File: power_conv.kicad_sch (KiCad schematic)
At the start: 28 parts, among them IC1 MAX17262HEWL+T, U10 TPS22916CNYFPR, U7 TPS62840YBGR, U8 TPS62840YBGR

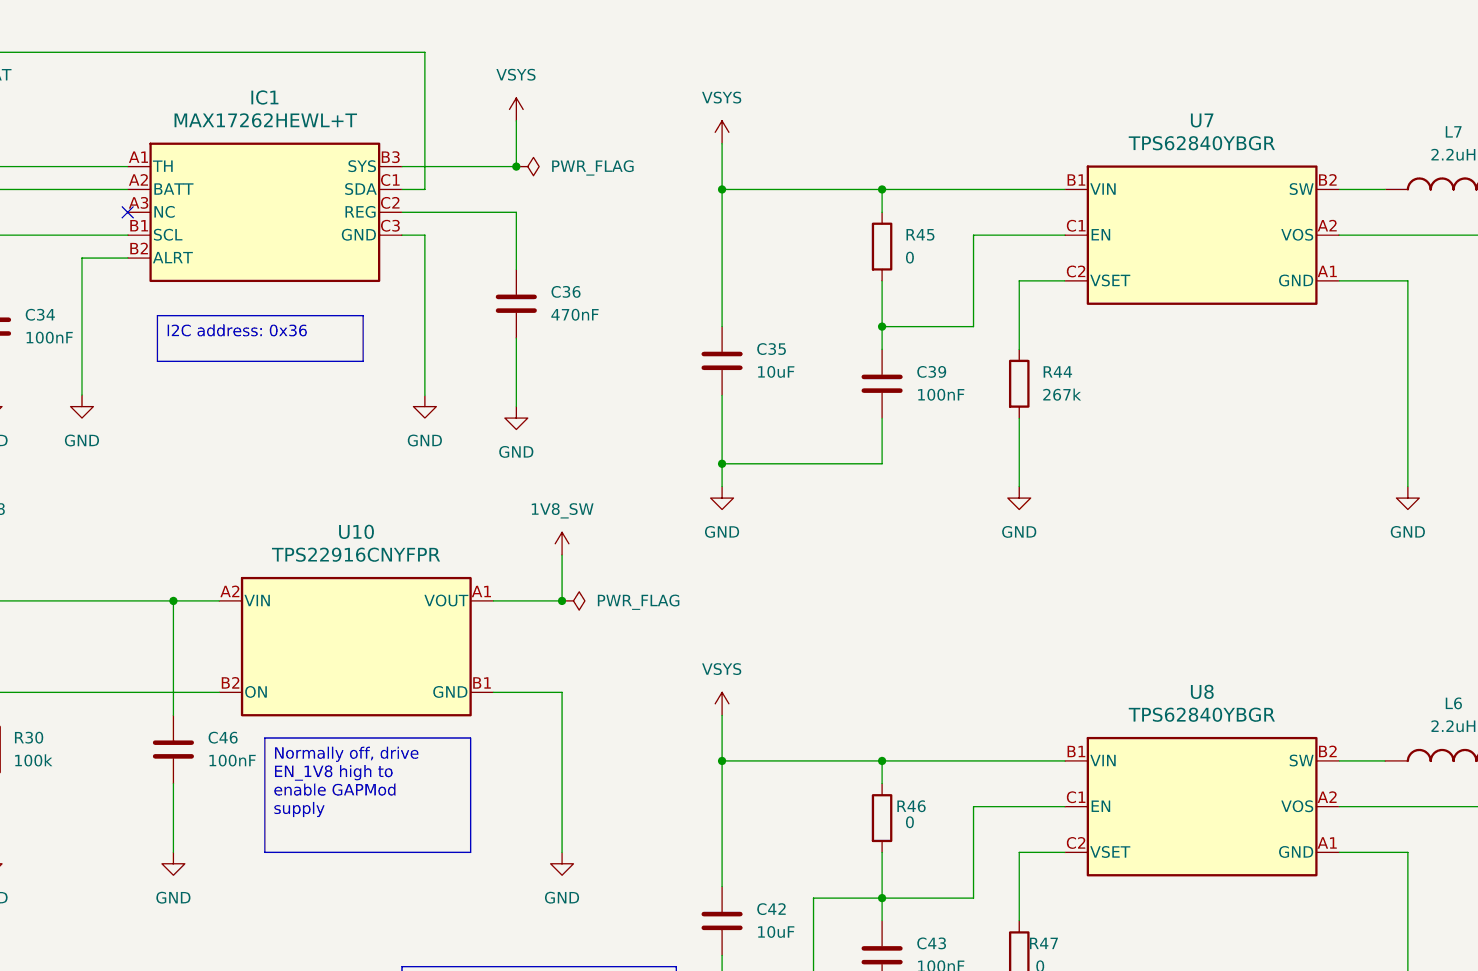
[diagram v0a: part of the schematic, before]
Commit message: added schematics comments of review 1
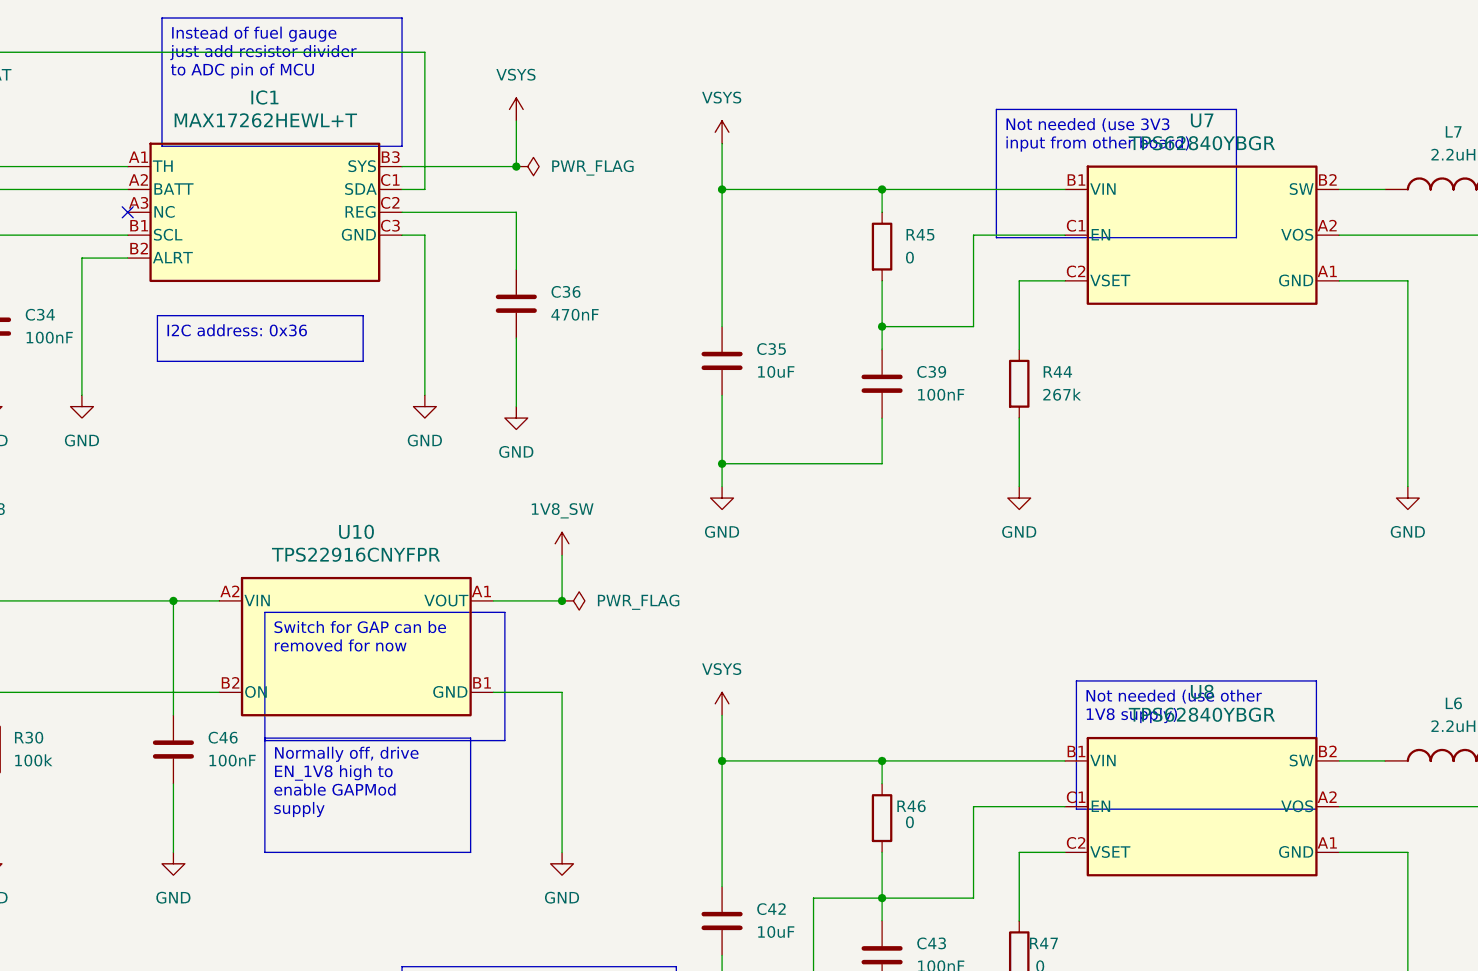
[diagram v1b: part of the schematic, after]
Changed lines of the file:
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@@
+		)
+	)
+	(text_box "Not needed (use 3V3 input from other board) "
+		(exclude_from_sim no)
+		(at 172.72 31.75 0)
+		(size 26.67 14.2494)
+		(margins 0.9525 0.9525 0.9525 0.9525)
+		(stroke
+			(width 0)
+			(type solid)
+		)
+		(fill
+			(type color)
+			(color 255 153 0 1)
+		)
+		(effects
+			(font
+				(size 1.27 1.27)
+			)
+			(justify left top)
 		)
 	)
@@
 			(type color)
 			(color 255 255 150 1)
+		)
+		(effects
+			(font
+				(size 1.27 1.27)
+			)
+			(justify left top)
+		)
+	)
+	(text_box "Not needed (use other 1V8 supply) "
+		(exclude_from_sim no)
+		(at 181.61 95.25 0)
+		(size 26.67 14.2494)
+		(margins 0.9525 0.9525 0.9525 0.9525)
+		(stroke
+			(width 0)
+			(type solid)
+		)
+		(fill
+			(type color)
+			(color 255 153 0 1)
 		)
 		(effects
@@
 		)
 		(effects
+			(font
+				(size 1.27 1.27)
+			)
+			(justify left top)
+		)
+	)
+	(text_box "Switch for GAP can be removed for now"
+		(exclude_from_sim no)
+		(at 91.44 87.63 0)
+		(size 26.67 14.2494)
+		(margins 0.9525 0.9525 0.9525 0.9525)
+		(stroke
+			(width 0)
+			(type solid)
+		)
+		(fill
+			(type color)
+			(color 255 153 0 1)
+		)
+		(effects
+			(font
+				(size 1.27 1.27)
+			)
+			(justify left top)
+		)
+	)
+	(text_box "Instead of fuel gauge just add resistor divider to ADC pin of MCU"
+		(exclude_from_sim no)
+		(at 80.01 21.59 0)
+		(size 26.67 14.2494)
+		(margins 0.9525 0.9525 0.9525 0.9525)
+		(stroke
+			(width 0)
+			(type solid)
+		)
+		(fill
+			(type color)
+			(color 255 153 0 1)
+		)
+		(effects

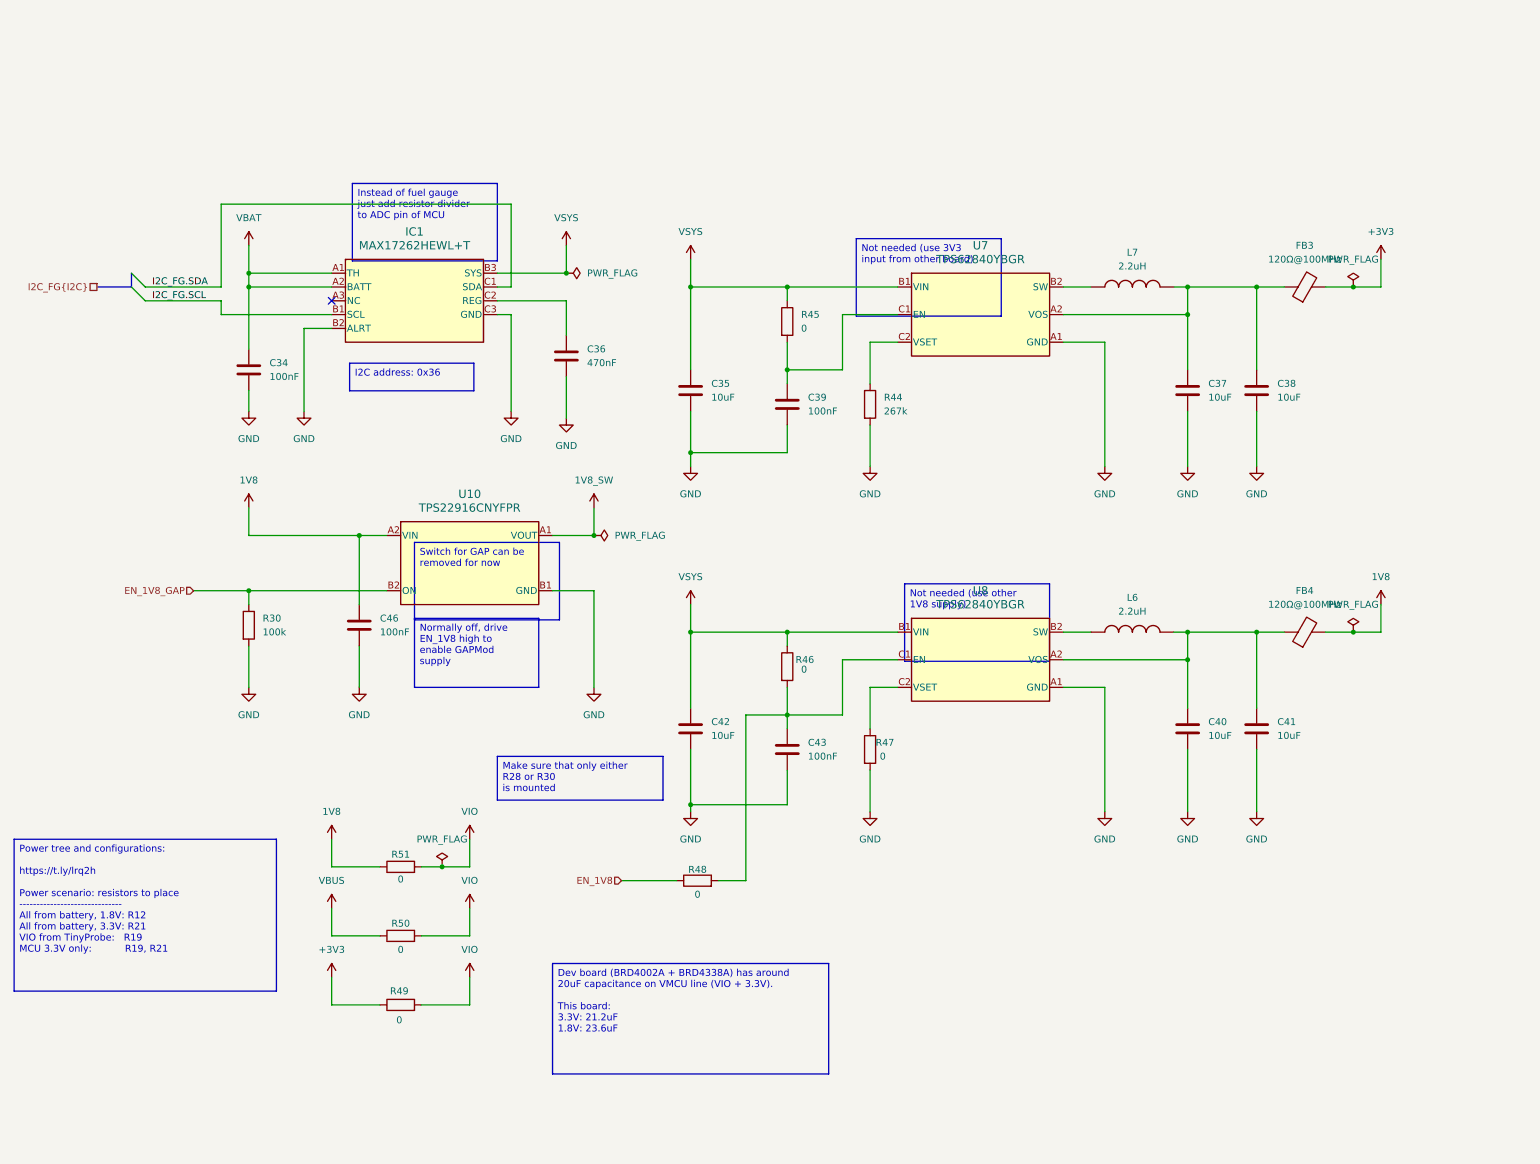
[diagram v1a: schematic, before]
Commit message: changes after first review: add lvl shifters, board at 1v8, new power tree
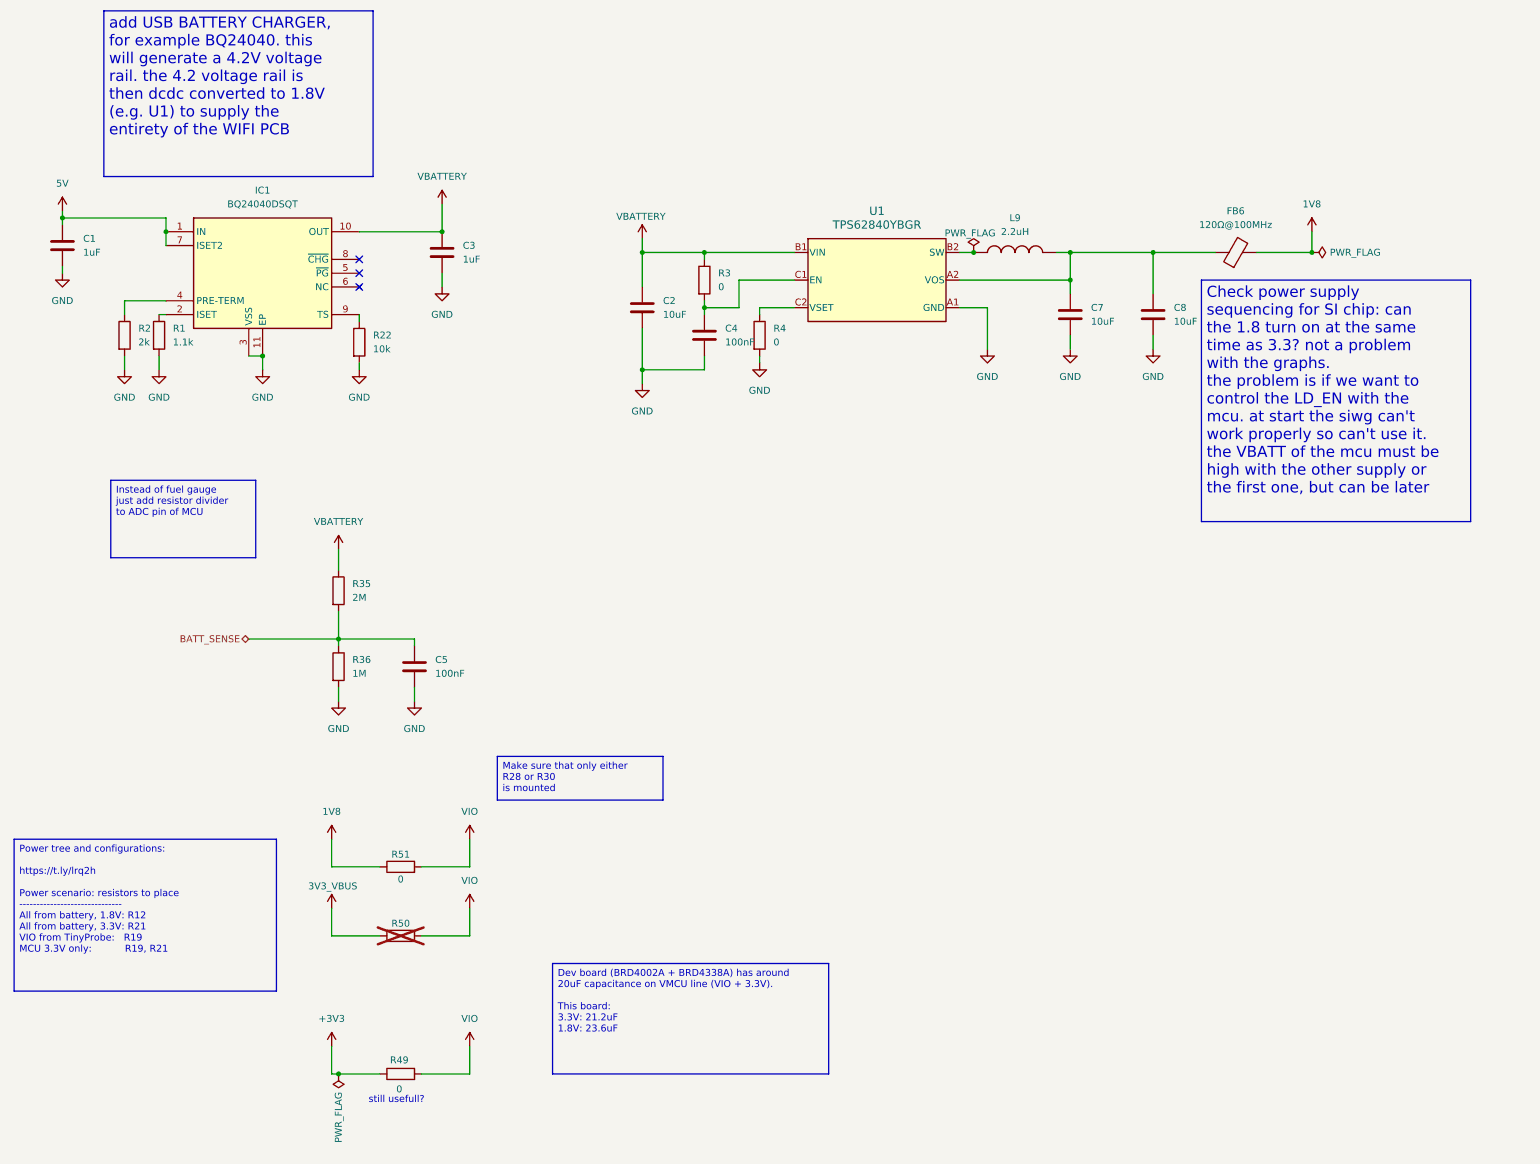
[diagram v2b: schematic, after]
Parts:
- removed C34, C39, C43, C46: 100nF, Capacitor_SMD:C_0402_1005Metric, symbol #dzdb:g_cap/C-100n-0402
- removed C35, C37, C38, C40, C41, C42: 10uF, Capacitor_SMD:C_0603_1608Metric, symbol #dzdb:g_cap/C-10u-0603
- removed C36: 470nF, Capacitor_SMD:C_0402_1005Metric, symbol #dzdb:g_cap/C-470n-0402
- removed FB3, FB4: 120Ω@100MHz, dz_ind:BLM15KD121SN1D, symbol #dzdb:s_ind/L-FB-120R-1.5A-0402
- removed IC1: MAX17262HEWL+T, dz_pwr:MAX17262HEWL+, symbol #dzdb:s_pwr/P-ADI-MAX17262HEWL
- removed L6, L7: 2.2uH, dz_ind:DFE2MCAH2R2MJ0L, symbol #dzdb:s_ind/L-2.2uH-1.4A-0806
- removed R30: 100k, Resistor_SMD:R_0402_1005Metric, symbol #dzdb:g_res/R-100k-0402
- removed R44: 267k, Resistor_SMD:R_0402_1005Metric, symbol #dzdb:g_res/R-267K-0402
- removed R45, R46, R47, R48: 0, Resistor_SMD:R_0402_1005Metric, symbol #dzdb:g_res/R-0-0402
- removed U10: TPS22916CNYFPR, dz_pwr:TPS22916CNYFPR, symbol #dzdb:s_pwr/P-TI-TPS22916CNYFPR
- removed U7, U8: TPS62840YBGR, dz_pwr:DSBGA6_1P4XP9_TEX, symbol #dzdb:s_pwr/P-TI-TPS62840YBGR
- added C1, C3: 1uF, Capacitor_SMD:C_0402_1005Metric, symbol #dzdb:g_cap/C-1u-0402
- added C2, C7, C8: 10uF, Capacitor_SMD:C_0603_1608Metric, symbol #dzdb:g_cap/C-10u-0603
- added C4, C5: 100nF, Capacitor_SMD:C_0402_1005Metric, symbol #dzdb:g_cap/C-100n-0402
- added FB6: 120Ω@100MHz, dz_ind:BLM15KD121SN1D, symbol #dzdb:s_ind/L-FB-120R-1.5A-0402
- added IC1: BQ24040DSQT, dz_pwr:BQ24040DSQT, symbol #dzdb:s_pwr/P-TI-BQ24040DSQT
- added L9: 2.2uH, dz_ind:DFE2MCAH2R2MJ0L, symbol #dzdb:s_ind/L-2.2uH-1.4A-0806
- added R1: 1.1k, Resistor_SMD:R_0402_1005Metric, symbol #dzdb:s_res/R-S-YAE-RT0402BRE071K1L
- added R2: 2k, Resistor_SMD:R_0402_1005Metric, symbol #dzdb:s_res/R-S-YAE-RT0402DRD072KL
- added R22: 10k, Resistor_SMD:R_0402_1005Metric, symbol #dzdb:g_res/R-10k-0402
- added R3, R4: 0, Resistor_SMD:R_0402_1005Metric, symbol #dzdb:g_res/R-0-0402
- added R35: 2M, Resistor_SMD:R_0402_1005Metric, symbol #dzdb:g_res/R-2M-0402
- added R36: 1M, Resistor_SMD:R_0402_1005Metric, symbol #dzdb:g_res/R-1M-0402
- added U1: TPS62840YBGR, dz_pwr:DSBGA6_1P4XP9_TEX, symbol #dzdb:s_pwr/P-TI-TPS62840YBGR
- R50: now not fitted
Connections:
- net 1V8: now also FB6.2
- net GND: now also C1.2, C2.2, C3.2, C4.2, C5.2, C7.2, C8.2, IC1.11 (EP), IC1.3 (VSS), R1.2, R2.2, R22.2, R36.2, R4.2, U1.A1 (GND)
- net VBUS renamed 3V3_VBUS
- new net: C7.1, C8.1, FB6.1, L9.2, U1.A2 (VOS)
- new net: IC1.2 (ISET), R1.1
- new net: IC1.4 (PRE-TERM), R2.1
- new net: IC1.9 (TS), R22.1
- new net: C4.1, R3.2, U1.C1 (EN)
- new net: R4.1, U1.C2 (VSET)
- new net: L9.1, U1.B2 (SW)
- new net 5V: C1.1, IC1.1 (IN), IC1.7 (ISET2)
- new net BATT_SENSE: C5.1, R35.2, R36.1
- new net VBATTERY: C2.1, C3.1, IC1.10 (OUT), R3.1, R35.1, U1.B1 (VIN)
- no-connect marks 1 -> 3
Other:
- note added: "still usefull?"
- moved on the sheet: R49

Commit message: updated schematic and initial pcb placement
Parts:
- removed R35: 2M, Resistor_SMD:R_0402_1005Metric, symbol #dzdb:g_res/R-2M-0402
- removed R36: 1M, Resistor_SMD:R_0402_1005Metric, symbol #dzdb:g_res/R-1M-0402
- removed R49: 0, Resistor_SMD:R_0402_1005Metric, symbol #dzdb:g_res/R-0-0402
- added R30: 100k, Resistor_SMD:R_0402_1005Metric, symbol #dzdb:g_res/R-100k-0402
- added R35: 220k, Resistor_SMD:R_0402_1005Metric, symbol #dzdb:g_res/R-220k-0402
- U1: footprint dz_pwr:DSBGA6_1P4XP9_TEX -> Package_BGA:Texas_DSBGA-6_0.9x1.4mm_Layout2x3_P0.5mm
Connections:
- net BATT_SENSE: now also R30.1, R35.2
- net GND: now also R30.2
- net VBATTERY: now also R35.1
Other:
- note added: "change value to 100 k"
- note removed: "still usefull?"
